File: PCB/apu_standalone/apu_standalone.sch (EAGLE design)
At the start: 95 parts, among them IC1 74AHC573, IC10 DAC, IC11 IS62C1024AL, IC12 ATMEGA2560, IC15 FT232RL, IC2 4050D, IC3 DS1307, IC4 LP298XS, IC5 S-SMP, IC6 S-DSP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

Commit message: reorganize directory structure
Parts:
- renumbered C32 to C29, C33 to C30, C34 to C31
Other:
- moved on the sheet: C15, C16, C17, C18, C19, C22, C23

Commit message: schematic sheets used more effectively.
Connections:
- net GND: now also IC15.GND; no longer IC12.GND1, IC12.GND2, IC12.GND3, IC15.GND1, IC15.GND2, IC15.GND3
- net VCC: no longer IC12.VCC1, IC12.VCC2, IC12.VCC3
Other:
- note removed: "SNES Audio Processing Unit"

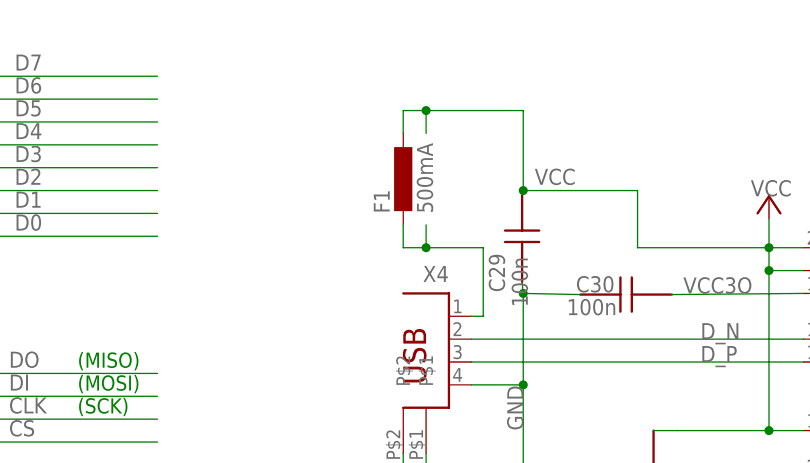
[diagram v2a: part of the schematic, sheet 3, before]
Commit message: Change out PTC fuse for better clearance.
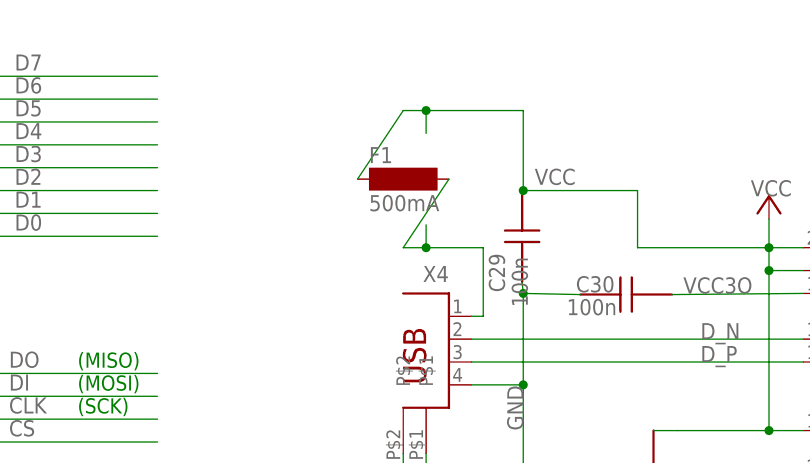
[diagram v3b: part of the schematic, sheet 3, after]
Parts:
- F1: device rcl:L-EUL1812 -> inductor-neosid:SM-1206
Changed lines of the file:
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@@
 <part name="IC15" library="SmartPrj" deviceset="FT232RL" device=""/>
 <part name="X4" library="SmartPrj" deviceset="PN61729" device=""/>
-<part name="F1" library="rcl" deviceset="L-EU" device="L1812" value="500mA"/>
+<part name="F1" library="inductor-neosid" deviceset="SM-1206" device="" value="500mA"/>
 <part name="C31" library="apu_pcb" deviceset="C0805" device="" value="100n"/>
 <part name="GND28" library="supply1" deviceset="GND" device=""/>
@@
 <wire x1="227.965" y1="166.37" x2="238.76" y2="166.37" width="0.1524" layer="91"/>
 <wire x1="227.965" y1="166.37" x2="225.425" y2="166.37" width="0.1524" layer="91"/>
-<wire x1="225.425" y1="166.37" x2="225.425" y2="163.83" width="0.1524" layer="91"/>
+<wire x1="225.425" y1="166.37" x2="220.345" y2="158.75" width="0.1524" layer="91"/>
 <junction x="238.76" y="157.48"/>
 <junction x="227.965" y="166.37"/>
@@
 <wire x1="233.045" y1="143.51" x2="234.315" y2="143.51" width="0.1524" layer="91"/>
 <wire x1="227.965" y1="151.13" x2="225.425" y2="151.13" width="0.1524" layer="91"/>
-<wire x1="225.425" y1="151.13" x2="225.425" y2="153.67" width="0.1524" layer="91"/>
+<wire x1="225.425" y1="151.13" x2="230.505" y2="158.75" width="0.1524" layer="91"/>
 <junction x="227.965" y="151.13"/>
 <pinref part="F1" gate="G$1" pin="2"/>
